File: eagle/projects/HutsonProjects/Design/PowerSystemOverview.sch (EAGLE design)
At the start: 28 parts, among them U1 MCP7384XX, U3 MT3608, U4 LTC3531ES6-3_3

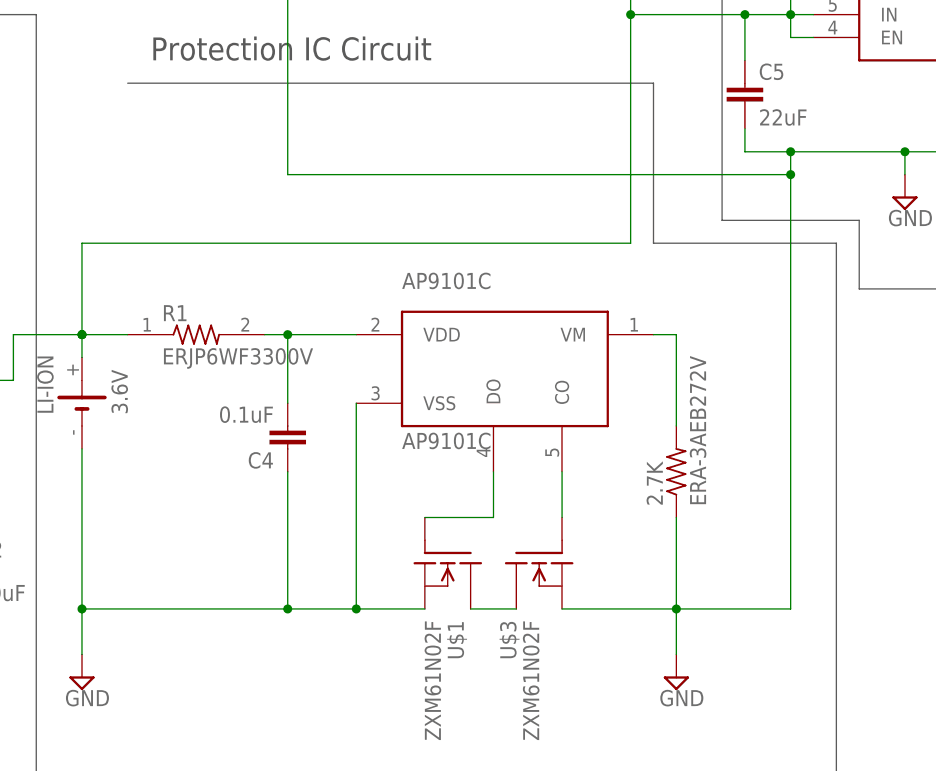
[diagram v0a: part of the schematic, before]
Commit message: 2.7k chip resistor
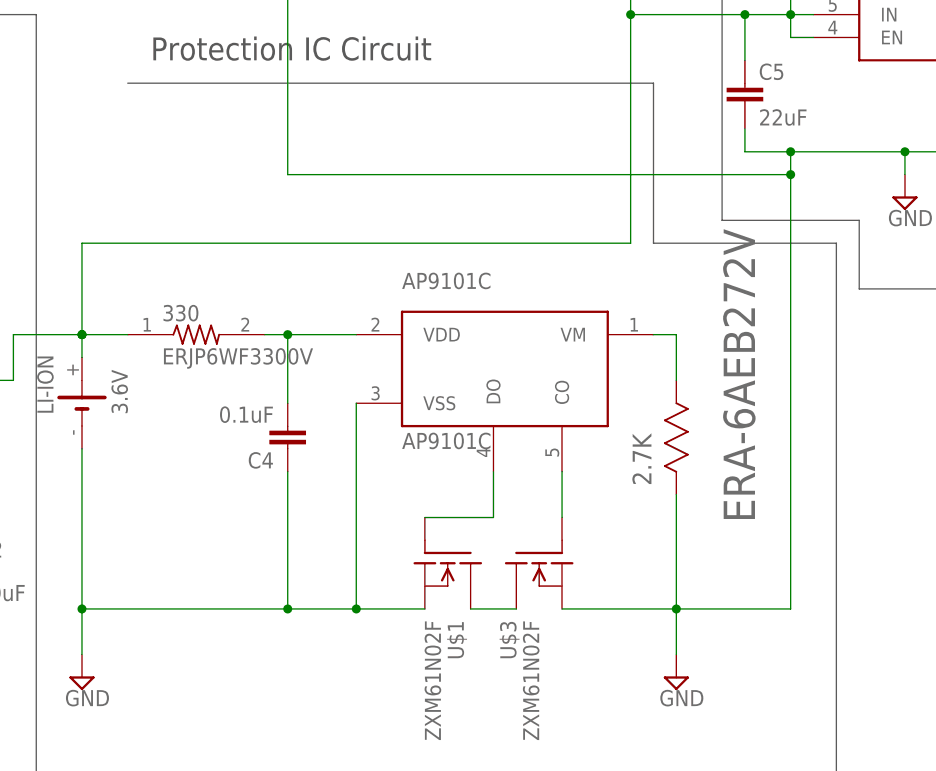
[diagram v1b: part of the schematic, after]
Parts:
- 2.7K: value ERA-3AEB272V -> ERA-6AEB272V; device ERA-3AEB272V:ERA-3AEB272V -> ERA-6AEB272V:ERA-6AEB272V
- renumbered R1 to 330
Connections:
- net GND: now also 2.7K.R2; no longer 2.7K.1
- net N$9: now also 2.7K.R1; no longer 2.7K.2
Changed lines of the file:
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@@
 <part name="U$6" library="DB2W31900L" deviceset="DB2W31900" device=""/>
 <part name="0.1OHM" library="RL1220S-R10-F" deviceset="RL1220S-R10-F" device=""/>
-<part name="2.7K" library="ERA-3AEB272V" deviceset="ERA-3AEB272V" device=""/>
 <part name="5V_USB" library="10118193-0001LF" deviceset="10118193-0001LF" device=""/>
 <part name="SUPPLY6" library="supply2" library_urn="urn:adsk.eagle:library:372" deviceset="GND" device=""/>
 <part name="100K" library="CRGH0805J100K" deviceset="CRGH0805J100K" device=""/>
-<part name="R1" library="ERJP6WF3300V" deviceset="ERJP6WF3300V" device=""/>
+<part name="330" library="ERJP6WF3300V" deviceset="ERJP6WF3300V" device=""/>
+<part name="2.7K" library="ERA-6AEB272V" deviceset="ERA-6AEB272V" device=""/>
 </parts>
 <sheets>
@@
 <attribute name="NAME" x="-6.628359375" y="109.451509375" size="2.084990625" layer="95" ratio="10" rot="SR0"/>
 </instance>
-<instance part="2.7K" gate="G$1" x="154.94" y="96.52" smashed="yes" rot="R90">
-<attribute name="NAME" x="153.44091875" y="92.708790625" size="1.77856875" layer="95" rot="R90"/>
-<attribute name="VALUE" x="158.242209375" y="92.709759375" size="1.778109375" layer="96" rot="R90"/>
-</instance>
 <instance part="5V_USB" gate="G$1" x="-91.44" y="101.6" smashed="yes" rot="R180">
 <attribute name="NAME" x="-86.35835" y="90.6714" size="1.778" layer="95" rot="R180"/>
@@
 <attribute name="VALUE" x="8.89" y="77.978" size="1.778" layer="96"/>
 </instance>
-<instance part="R1" gate="G$1" x="101.6" y="111.76" smashed="yes">
+<instance part="330" gate="G$1" x="101.6" y="111.76" smashed="yes">
 <attribute name="NAME" x="97.79" y="113.2586" size="1.778" layer="95"/>
 <attribute name="VALUE" x="97.79" y="108.458" size="1.778" layer="96"/>
+</instance>
+<instance part="2.7K" gate="A" x="154.94" y="93.98" smashed="yes" rot="R90">
+<attribute name="VALUE" x="163.6776" y="90.8558" size="3.4798" layer="96" ratio="10" rot="SR90"/>
+<attribute name="NAME" x="152.1714" y="94.9706" size="2.0828" layer="95" ratio="10" rot="SR90"/>
 </instance>
 </instances>
@@
 <junction x="111.76" y="185.42"/>
 <junction x="167.64" y="129.54"/>
-<pinref part="2.7K" gate="G$1" pin="1"/>
-<wire x1="154.94" y1="91.44" x2="154.94" y2="81.28" width="0.1524" layer="91"/>
+<pinref part="2.7K" gate="A" pin="R2"/>
+<wire x1="154.94" y1="93.98" x2="154.94" y2="81.28" width="0.1524" layer="91"/>
 </segment>
 <segment>
@@
 <wire x1="111.76" y1="111.76" x2="119.38" y2="111.76" width="0.1524" layer="91"/>
 <wire x1="111.76" y1="104.14" x2="111.76" y2="111.76" width="0.1524" layer="91"/>
-<pinref part="R1" gate="G$1" pin="2"/>
+<pinref part="330" gate="G$1" pin="2"/>
 <wire x1="109.22" y1="111.76" x2="111.76" y2="111.76" width="0.1524" layer="91"/>
 <junction x="111.76" y="111.76"/>
@@
 <wire x1="83.82" y1="213.36" x2="111.76" y2="213.36" width="0.1524" layer="91"/>
 <junction x="111.76" y="213.36"/>
-<pinref part="R1" gate="G$1" pin="1"/>
+<pinref part="330" gate="G$1" pin="1"/>
 <wire x1="88.9" y1="111.76" x2="93.98" y2="111.76" width="0.1524" layer="91"/>
 <junction x="88.9" y="111.76"/>
@@
 <pinref part="U$4" gate="G$1" pin="VM"/>
 <wire x1="152.4" y1="111.76" x2="154.94" y2="111.76" width="0.1524" layer="91"/>
-<pinref part="2.7K" gate="G$1" pin="2"/>
-<wire x1="154.94" y1="111.76" x2="154.94" y2="101.6" width="0.1524" layer="91"/>
-</segment>
-</net>
+<pinref part="2.7K" gate="A" pin="R1"/>
+<wire x1="154.94" y1="111.76" x2="154.94" y2="106.68" width="0.1524" layer="91"/>
+</segment>
+</net>

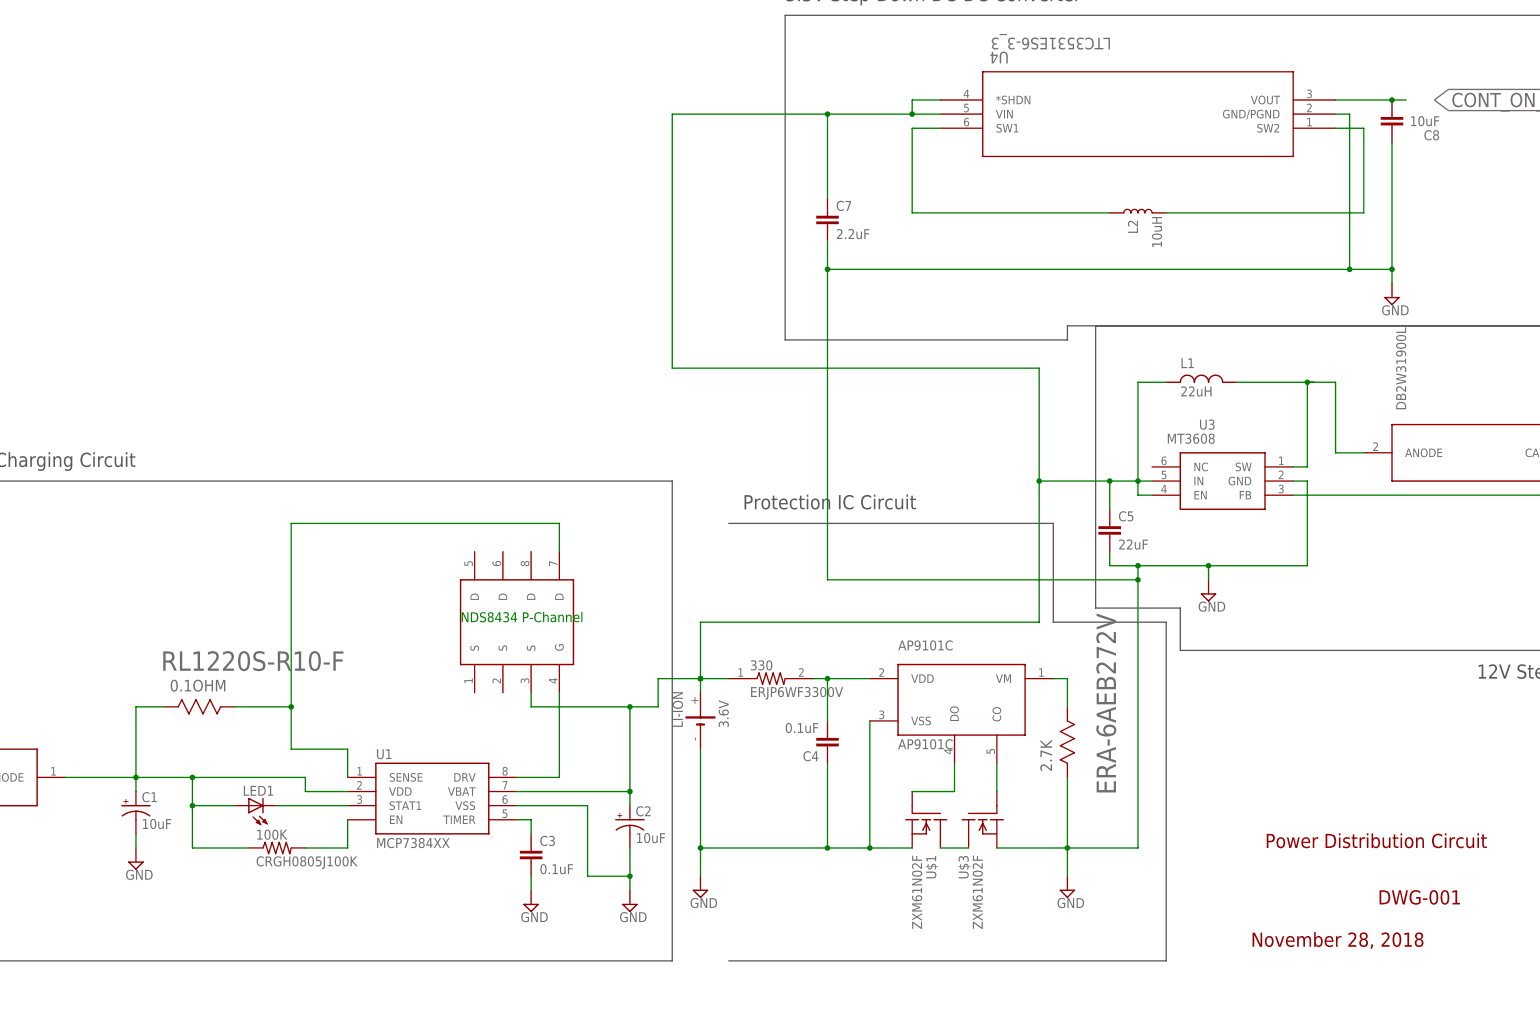
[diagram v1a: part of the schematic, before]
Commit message: Capacitor Chips Added
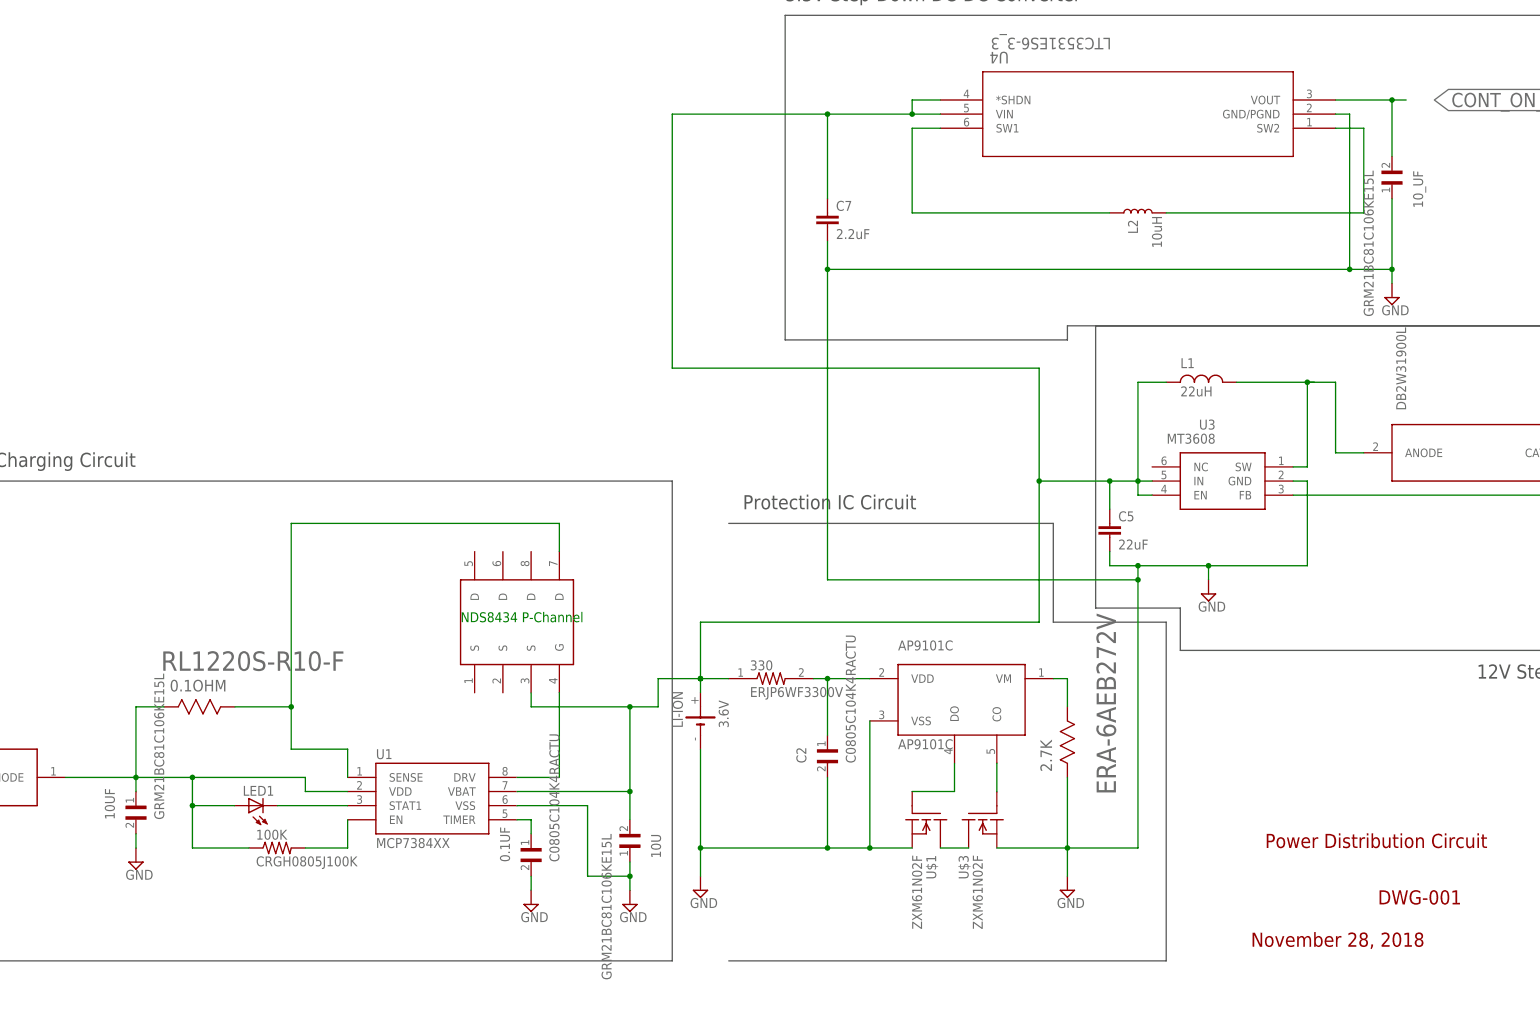
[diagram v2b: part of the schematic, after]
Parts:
- removed C1: 10uF, SparkFun-Capacitors:10UF-POLAR-0603-6.3V-20%(TANT)
- removed C3, C4: 0.1uF, SparkFun-Capacitors:0.1UF-0402-16V-10%
- removed C8: 10uF, SparkFun-Capacitors:10UF-0603-6.3V-20%
- added 0.1UF: C0805C104K4RACTU, C0805C104K4RACTU:C0805C104K4RACTU
- added 10U, 10UF, 10_UF: GRM21BC81C106KE15L, GRM21BC81C106KE15L:GRM21BC81C106KE15L
- C2: value 10uF -> C0805C104K4RACTU; device SparkFun-Capacitors:10UF-POLAR-0603-6.3V-20%(TANT) -> C0805C104K4RACTU:C0805C104K4RACTU
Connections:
- net CONT_ON_EMBEDDED: now also 10_UF.2; no longer C8.2
- net GND: now also 0.1UF.2, 10U.1, 10UF.2, 10_UF.1, C2.2; no longer C1.-, C2.-, C3.2, C4.1, C8.1
- net N$16: now also 10U.2; no longer C2.+
- net N$3: now also 10UF.1; no longer C1.+
- net N$6: now also 0.1UF.1; no longer C3.1
- net N$7: now also C2.1; no longer C4.2
